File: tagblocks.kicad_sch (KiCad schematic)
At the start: 6 parts

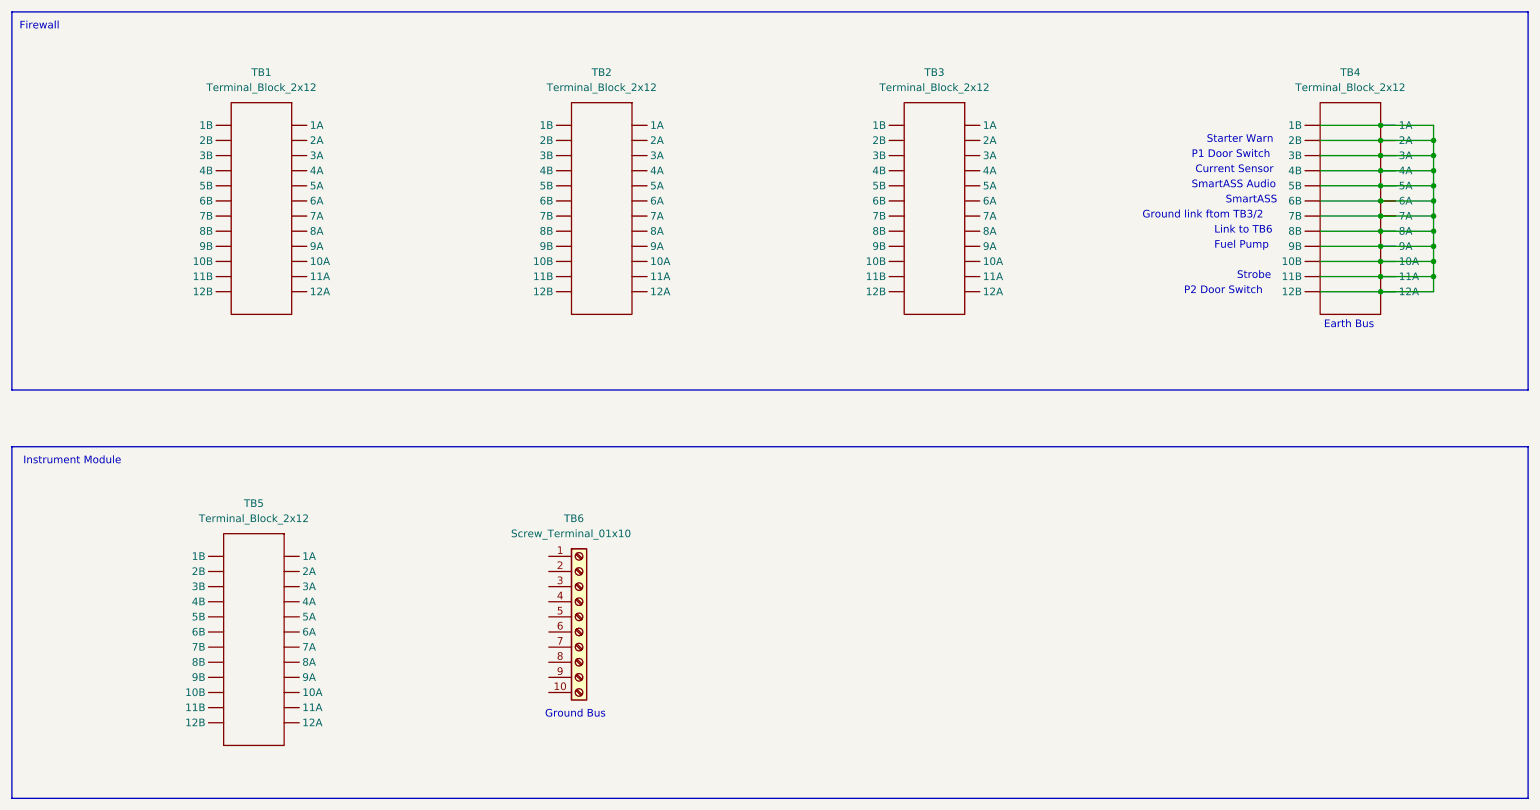
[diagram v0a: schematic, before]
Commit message: Updates from manual validation
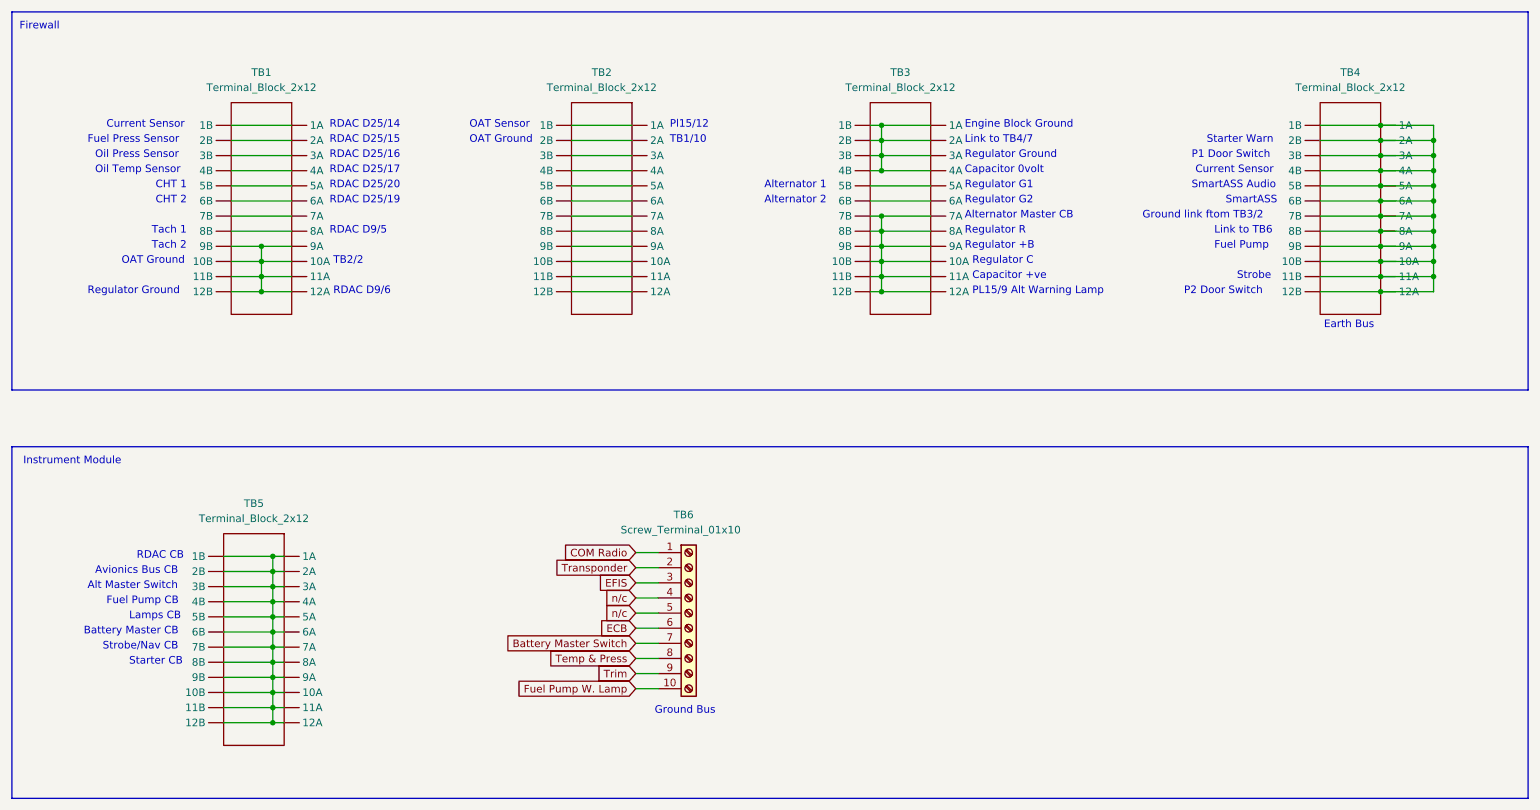
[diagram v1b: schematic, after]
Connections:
- net COM Radio: now reaches TB6.1 (Pin_1)
- net Fuel Pump W. Lamp: now reaches TB6.10 (Pin_10)
- net Transponder: now reaches TB6.2 (Pin_2)
- net EFIS: now reaches TB6.3 (Pin_3)
- net n/c: now reaches TB6.4 (Pin_4)
- net n/c: now also TB6.5 (Pin_5)
- net ECB: now reaches TB6.6 (Pin_6)
- net Battery Master Switch: now reaches TB6.7 (Pin_7)
- net Temp & Press: now reaches TB6.8 (Pin_8)
- net Trim: now reaches TB6.9 (Pin_9)
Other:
- note added: "Alt Master Switch"
- note added: "Alternator 1"
- note added: "Alternator 2"
- note added: "Alternator Master CB"
- note added: "Avionics Bus CB"
- note added: "Battery Master CB"
- note added: "CHT 1"
- note added: "CHT 2"
- note added: "Capacitor +ve"
- note added: "Capacitor 0volt"
- note added: "Engine Block Ground"
- note added: "Fuel Press Sensor"
- note added: "Fuel Pump CB"
- note added: "Lamps CB"
- note added: "Link to TB4/7"
- note added: "OAT Ground"
- note added: "OAT Sensor"
- note added: "Oil Press Sensor"
- note added: "Oil Temp Sensor"
- note added: "PL15/9 Alt Warning Lamp"
- note added: "Pl15/12"
- note added: "RDAC CB"
- note added: "RDAC D25/14"
- note added: "RDAC D25/15"
- note added: "RDAC D25/16"
- note added: "RDAC D25/17"
- note added: "RDAC D25/19"
- note added: "RDAC D25/20"
- note added: "RDAC D9/5"
- note added: "RDAC D9/6"
- note added: "Regulator +B"
- note added: "Regulator C"
- note added: "Regulator G1"
- note added: "Regulator G2"
- note added: "Regulator Ground"
- note added: "Regulator R"
- note added: "Starter CB"
- note added: "Strobe/Nav CB"
- note added: "TB1/10"
- note added: "TB2/2"
- note added: "Tach 1"
- note added: "Tach 2"
- moved on the sheet: TB3, TB6

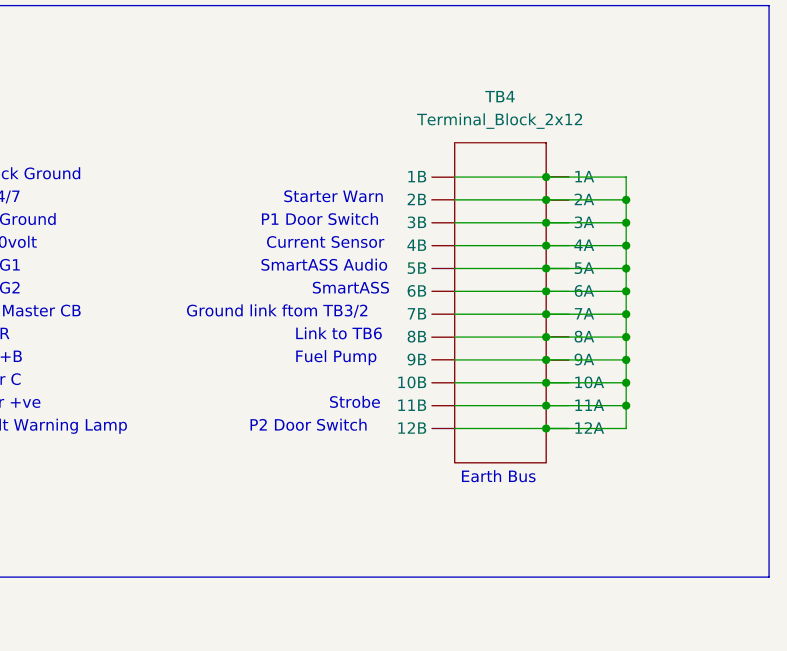
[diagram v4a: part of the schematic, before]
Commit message: Added fuel flow sensor ground connection
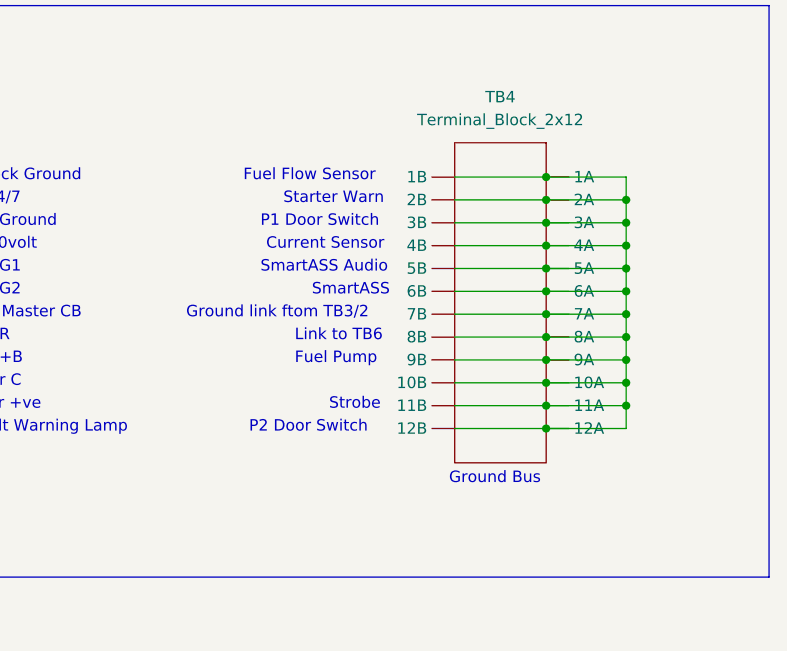
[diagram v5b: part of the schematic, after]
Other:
- note added: "Fuel Flow Sensor"
- note removed: "Earth Bus"
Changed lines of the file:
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@@
   (title_block
     (title "Europa - Electrical Tag Blocks")
-    (date "2022-12-24")
-    (rev "1")
+    (date "2023-01-03")
+    (rev "2")
   )
   (junction (at 165.1 54.61) (diameter 0) (color 0 0 0 0)
@@
     (effects (font (size 1.27 1.27)) (justify left bottom))
   )
-  (text "Earth Bus" (at 239.395 71.12 0)
+  (text "Ground Bus" (at 238.125 71.12 0)
     (effects (font (size 1.27 1.27)) (justify left bottom))
   )
@@
     (effects (font (size 1.27 1.27)) (justify left bottom))
   )
+  (text "Fuel Flow Sensor" (at 215.265 37.465 0)
+    (effects (font (size 1.27 1.27)) (justify left bottom))
+  )

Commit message: Catchup
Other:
- note added: "Ground link from TB3/2"
- note removed: "Ground link ftom TB3/2"
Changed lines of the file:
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@@
     (effects (font (size 1.27 1.27)) (justify left bottom))
   )
-  (text "Ground link ftom TB3/2" (at 208.915 52.705 0)
+  (text "Ground link from TB3/2" (at 208.915 52.705 0)
     (effects (font (size 1.27 1.27)) (justify left bottom))
   )
